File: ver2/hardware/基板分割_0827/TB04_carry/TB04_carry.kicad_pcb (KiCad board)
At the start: 2 copper layers, 100 x 30 mm, 10 parts, among them J1602 Screw_Terminal_01x02, J2 Conn_02x10_Odd_Even, J3 Conn_02x05_Odd_Even, J4 Conn_02x05_Odd_Even, J5 Conn_02x05_Odd_Even, J6 Conn_02x05_Odd_Even

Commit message: ver2: 3分割のフットプリント設定完了・取付穴を追加・PCBを作り直し
- 新規コネクタ11件のフットプリントを設定(2x20/2x10ピンソケット・端子台)
- 演算板/制御板/キャリアに取付穴MountingHole_Pad×4とGNDを追加(M3・パッド付きビア)
- 3枚のPCBをコピー元マスターのレイアウトを一掃して作り直し(配置前・配線0)
- 階層から外れて残っていたRS00/RS01.kicad_sch(制御板・IF板)を削除

検証: フットプリント未設定0件、回路図とPCBの参照番号の集合差分0
(演算102/制御101/IF127/キャリア14)、回路図の電気的変更なし

Co-Authored-By: Claude Opus 5 <noreply@anthropic.com>
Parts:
- added H1: MountingHole_Pad, MountingHole:MountingHole_3.2mm_M3_Pad_Via, F.Cu at (158.5, 58.5)
- added H2: MountingHole_Pad, MountingHole:MountingHole_3.2mm_M3_Pad_Via, F.Cu at (158.5, 66.4)
- added H3: MountingHole_Pad, MountingHole:MountingHole_3.2mm_M3_Pad_Via, F.Cu at (158.5, 74.4)
- added H4: MountingHole_Pad, MountingHole:MountingHole_3.2mm_M3_Pad_Via, F.Cu at (158.5, 82.3)

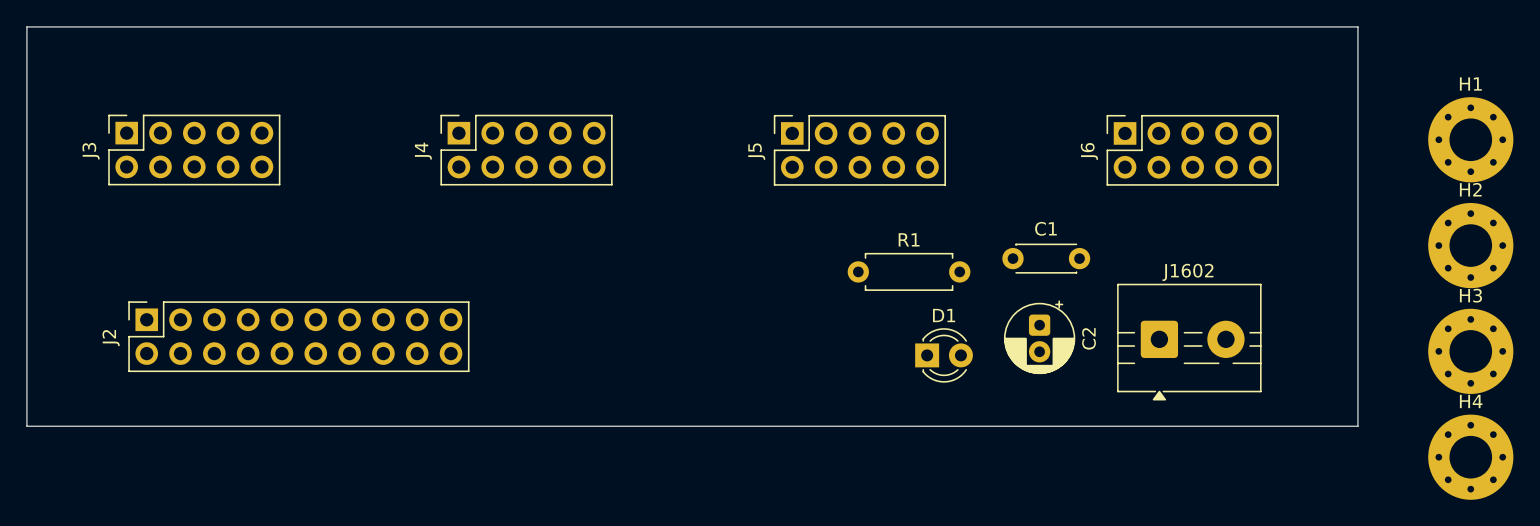
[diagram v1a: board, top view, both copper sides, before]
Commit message: ver2: キャリア基板のPCBが完成(査収済み)／IF板の取付穴を配置
キャリア(TB04_carry):
- 外形100x30・角R4、取付穴を四隅に配置
- 表示ソケットJ3-J6は25mmピッチで板の中心に一致
- トラック109本・ビア51個(幅0.20mm/0.80mm)、GNDベタを両面

査収(pcbnew APIで実測):
- DRC 違反0・未配線0
- 全14部品が外形の内側(最小余裕0.70mm)
- 7segIF実測23.05x41.55mm、4台で幅約98mm=100mm板に左右1mmずつ収まる

IF板: 取付穴H501/H502を外形内へ移動(作業中)

Co-Authored-By: Claude Opus 5 <noreply@anthropic.com>
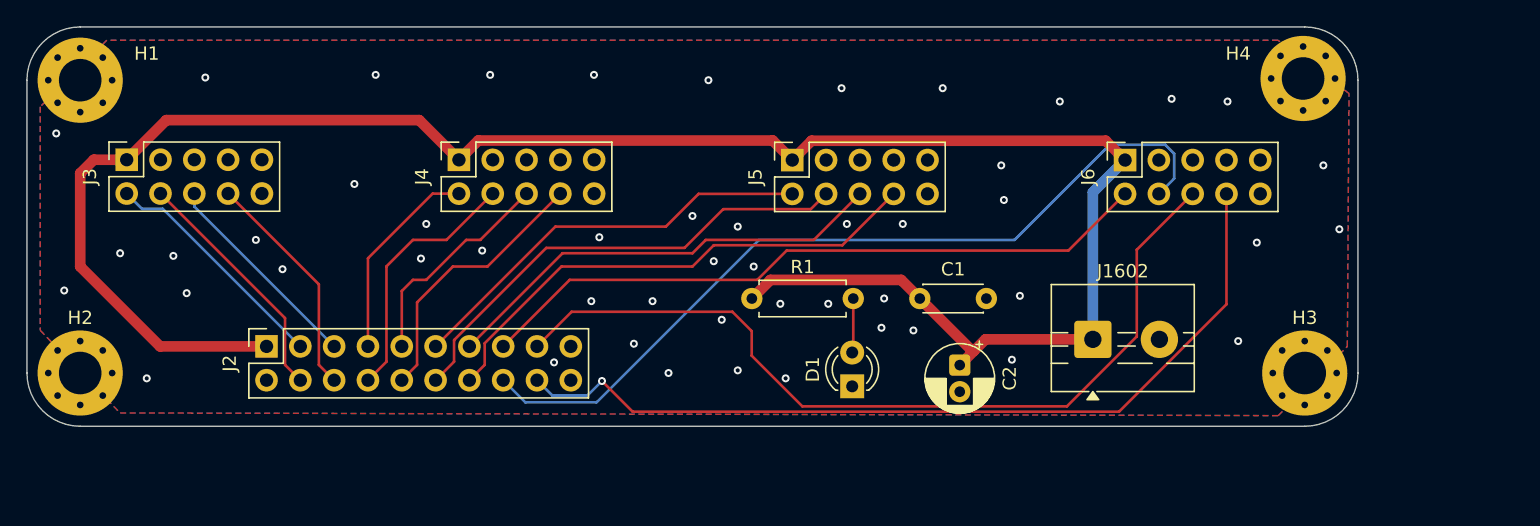
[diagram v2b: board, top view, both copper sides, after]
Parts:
- moved H2 104.9 mm to (54.0, 76.0)
- moved H1 104.6 mm to (54.0, 54.0)
- moved H4 31.1 mm to (145.9, 53.9)
- moved H3 12.6 mm to (146.0, 76.0)
- moved J2 9.22 mm to (68.0, 74.0)
- moved R1 8.25 mm to (104.5, 70.4)
- moved C1 7.62 mm to (117.1, 70.4)
- moved C2 6.71 mm to (120.1, 75.4)
- moved D1 6.09 mm to (112.0, 77.0), turned to 90 degrees
- moved J1602 5.00 mm to (130.1, 73.5)
- moved J3 2.00 mm to (57.5, 60.0)
- moved J4 2.00 mm to (82.5, 60.0)
- moved J5 2.00 mm to (107.5, 60.0)
- moved J6 2.00 mm to (132.5, 60.0)
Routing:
- net VDD: track 0.00 -> 152.0 mm
- net DIG_D3_0: track 0.00 -> 65.3 mm, vias 0 -> 1
- net DIG_D3_1: track 0.00 -> 64.8 mm
- net DIG_D3_2: track 0.00 -> 62.9 mm
- net DIG_D3_3: track 0.00 -> 51.5 mm
- net DIG_D2_0: track 0.00 -> 38.6 mm
- net DIG_D2_2: track 0.00 -> 36.1 mm
- net DIG_D2_1: track 0.00 -> 34.1 mm
- net DIG_D2_3: track 0.00 -> 31.5 mm
- net DIG_D1_0: track 0.00 -> 20.5 mm
- net DIG_D1_2: track 0.00 -> 19.4 mm
- net DIG_D0_2: track 0.00 -> 18.4 mm
- net DIG_D0_3: track 0.00 -> 17.8 mm
- net DIG_D0_0: track 0.00 -> 17.3 mm
- net DIG_D1_1: track 0.00 -> 16.6 mm
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- added copper zone on B.Cu, net GND
- added copper zone on F.Cu, net GND
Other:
- outline, holes or cut-outs redrawn
